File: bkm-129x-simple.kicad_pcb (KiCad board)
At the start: 2 copper layers, 105 x 89.3 mm, 52 parts, among them J1 YG1, J2 PBB1, J3 PRR1, J4 SYNC1, J5 Conn_02x32_Row_Letter_Last, Q1 DTC144EKA, U1 ADG1611, U2 THS7374, U3 arduino-nano-v3, U4 74LVC125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

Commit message: Added readme and some info on silkscreen
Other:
- board text added: "B-Y/B"
- board text added: "R-Y/R"
- board text added: "SYNC"
- board text added: "Y/G"
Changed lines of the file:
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@@
     (links 157)
     (no_connects 0)
-    (area 120.955999 61.773999 226.071501 151.205001)
+    (area 100.362599 61.652999 228.7352 151.453001)
     (thickness 1.6)
-    (drawings 10)
+    (drawings 14)
     (tracks 449)
     (zones 0)
@@
   (module bnc-tht:BNC-THT (layer F.Cu)
     (at 129.0066 73.4314)
-    (fp_text reference J1 (at 0 8.382) (layer F.SilkS)
+    (fp_text reference J1 (at 6.1214 -8.3439) (layer F.SilkS)
       (effects (font (size 1 1) (thickness 0.15)))
     )
@@
   (module bnc-tht:BNC-THT (layer F.Cu)
     (at 129.0066 95.4786)
-    (fp_text reference J2 (at 0 8.382) (layer F.SilkS)
+    (fp_text reference J2 (at 6.1214 -8.3566) (layer F.SilkS)
       (effects (font (size 1 1) (thickness 0.15)))
     )
@@
   (module bnc-tht:BNC-THT (layer F.Cu)
     (at 129.032 117.475)
-    (fp_text reference J3 (at 0 8.382) (layer F.SilkS)
+    (fp_text reference J3 (at 6.096 -8.382) (layer F.SilkS)
       (effects (font (size 1 1) (thickness 0.15)))
     )
@@
   (module bnc-tht:BNC-THT (layer F.Cu)
     (at 129.032 139.573)
-    (fp_text reference J4 (at 0 8.382) (layer F.SilkS)
+    (fp_text reference J4 (at 6.1595 -8.382) (layer F.SilkS)
       (effects (font (size 1 1) (thickness 0.15)))
     )
@@
     )
   )
+  (gr_text SYNC (at 133.096 148.463) (layer F.SilkS)
+    (effects (font (size 1.5 1.5) (thickness 0.3)))
+  )
+  (gr_text R-Y/R (at 132.1435 126.365) (layer F.SilkS)
+    (effects (font (size 1.5 1.5) (thickness 0.3)))
+  )
+  (gr_text B-Y/B (at 132.2705 104.4575) (layer F.SilkS)
+    (effects (font (size 1.5 1.5) (thickness 0.3)))
+  )
+  (gr_text Y/G (at 133.858 82.423) (layer F.SilkS)
+    (effects (font (size 1.5 1.5) (thickness 0.3)))
+  )
   (gr_text "(2020) Martin Hejnfelt (martin@hejnfelt.com)\nwww.immerhax.com" (at 171.9072 85.9536) (layer B.SilkS)

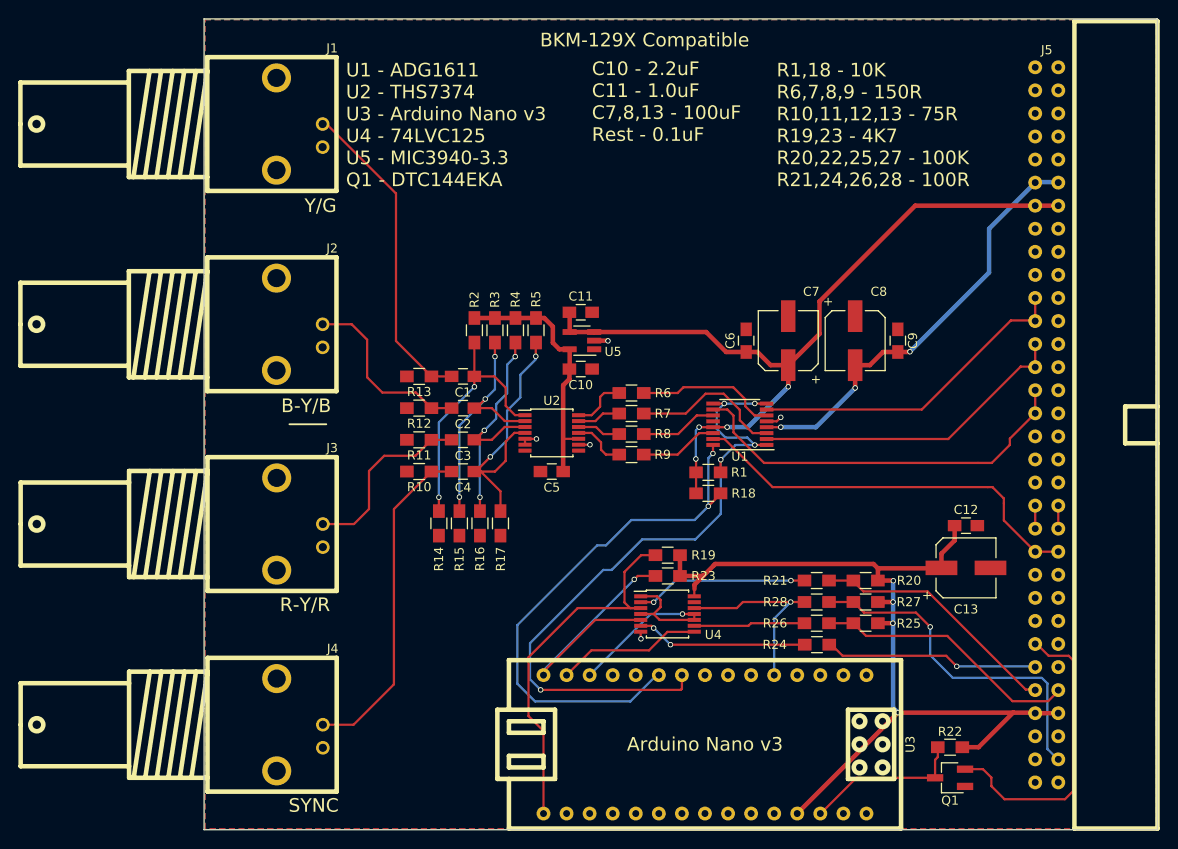
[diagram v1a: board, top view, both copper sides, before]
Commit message: Updated and fixed silkscreen BOM
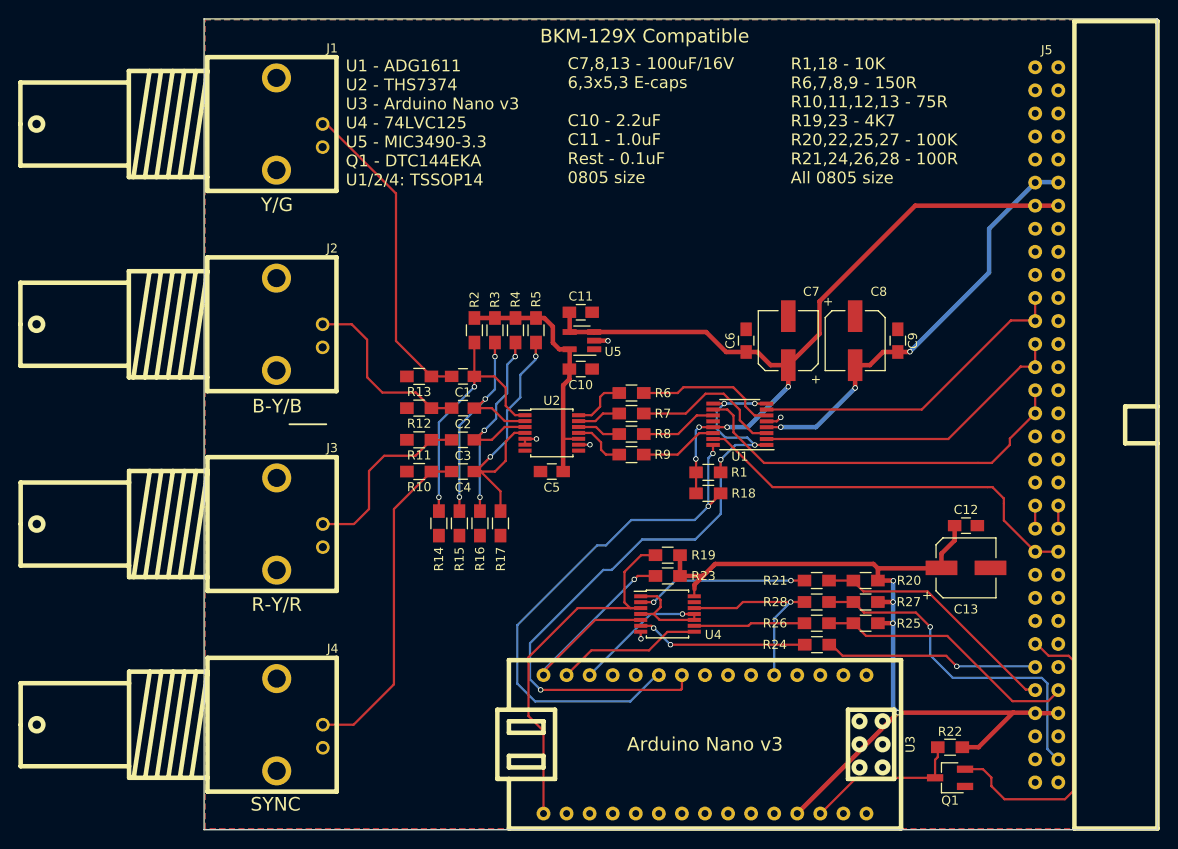
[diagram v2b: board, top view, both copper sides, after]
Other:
- board text added: "C7,8,13 - 100uF/16V 6,3x5,3 E-caps C10 - 2.2uF C11 - 1.0uF Rest - 0.1uF 0805 size"
- board text added: "R1,18 - 10K R6,7,8,9 - 150R R10,11,12,13 - 75R R19,23 - 4K7 R20,22,25,27 - 100K R21,24,26,28 - 100R All 0805 size"
- board text added: "U1 - ADG1611 U2 - THS7374 U3 - Arduino Nano v3 U4 - 74LVC125 U5 - MIC3490-3.3 Q1 - DTC144EKA U1/2/4: TSSOP14"
- board text removed: "C10 - 2.2uF C11 - 1.0uF C7,8,13 - 100uF Rest - 0.1uF"
- board text removed: "R1,18 - 10K R6,7,8,9 - 150R R10,11,12,13 - 75R R19,23 - 4K7 R20,22,25,27 - 100K R21,24,26,28 - 100R"
- board text removed: "U1 - ADG1611 U2 - THS7374 U3 - Arduino Nano v3 U4 - 74LVC125 U5 - MIC3940-3.3 Q1 - DTC144EKA"
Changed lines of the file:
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@@
     (links 157)
     (no_connects 0)
-    (area 100.362599 61.652999 228.7352 151.453001)
+    (area 120.955999 61.773999 226.071501 151.205001)
     (thickness 1.6)
     (drawings 14)
@@
     )
   )
-  (gr_text SYNC (at 133.096 148.463) (layer F.SilkS)
+  (gr_text SYNC (at 128.905 148.336) (layer F.SilkS)
     (effects (font (size 1.5 1.5) (thickness 0.3)))
   )
-  (gr_text R-Y/R (at 132.1435 126.365) (layer F.SilkS)
+  (gr_text R-Y/R (at 129.032 126.3396) (layer F.SilkS)
     (effects (font (size 1.5 1.5) (thickness 0.3)))
   )
-  (gr_text B-Y/B (at 132.2705 104.4575) (layer F.SilkS)
+  (gr_text B-Y/B (at 129.0828 104.4956) (layer F.SilkS)
     (effects (font (size 1.5 1.5) (thickness 0.3)))
   )
-  (gr_text Y/G (at 133.858 82.423) (layer F.SilkS)
+  (gr_text Y/G (at 129.0574 82.3214) (layer F.SilkS)
     (effects (font (size 1.5 1.5) (thickness 0.3)))
   )
@@
     (effects (font (size 1.5 1.5) (thickness 0.3)) (justify mirror))
   )
-  (gr_text "C10 - 2.2uF\nC11 - 1.0uF\nC7,8,13 - 100uF\nRest - 0.1uF" (at 163.7284 70.9676) (layer F.SilkS)
-    (effects (font (size 1.5 1.5) (thickness 0.3)) (justify left))
-  )
-  (gr_text "R1,18 - 10K\nR6,7,8,9 - 150R\nR10,11,12,13 - 75R\nR19,23 - 4K7\nR20,22,25,27 - 100K\nR21,24,26,28 - 100R" (at 184.0738 73.533) (layer F.SilkS)
-    (effects (font (size 1.5 1.5) (thickness 0.3)) (justify left))
-  )
-  (gr_text "U1 - ADG1611\nU2 - THS7374\nU3 - Arduino Nano v3\nU4 - 74LVC125\nU5 - MIC3940-3.3\nQ1 - DTC144EKA" (at 136.652 73.533) (layer F.SilkS)
-    (effects (font (size 1.5 1.5) (thickness 0.3)) (justify left))
-  )
-  (gr_text "BKM-129X Compatible" (at 169.545 64.1858) (layer F.SilkS)
+  (gr_text "C7,8,13 - 100uF/16V\n6,3x5,3 E-caps\n\nC10 - 2.2uF\nC11 - 1.0uF\nRest - 0.1uF\n0805 size\n" (at 161.0614 73.0504) (layer F.SilkS)
+    (effects (font (size 1.3 1.3) (thickness 0.25)) (justify left))
+  )
+  (gr_text "R1,18 - 10K\nR6,7,8,9 - 150R\nR10,11,12,13 - 75R\nR19,23 - 4K7\nR20,22,25,27 - 100K\nR21,24,26,28 - 100R\nAll 0805 size" (at 185.6232 73.0758) (layer F.SilkS)
+    (effects (font (size 1.3 1.3) (thickness 0.25)) (justify left))
+  )
+  (gr_text "U1 - ADG1611\nU2 - THS7374\nU3 - Arduino Nano v3\nU4 - 74LVC125\nU5 - MIC3490-3.3\nQ1 - DTC144EKA\nU1/2/4: TSSOP14" (at 136.6266 73.3044) (layer F.SilkS)
+    (effects (font (size 1.3 1.3) (thickness 0.25)) (justify left))
+  )
+  (gr_text "BKM-129X Compatible" (at 169.545 63.754) (layer F.SilkS)
     (effects (font (size 1.5 1.5) (thickness 0.3)))
   )

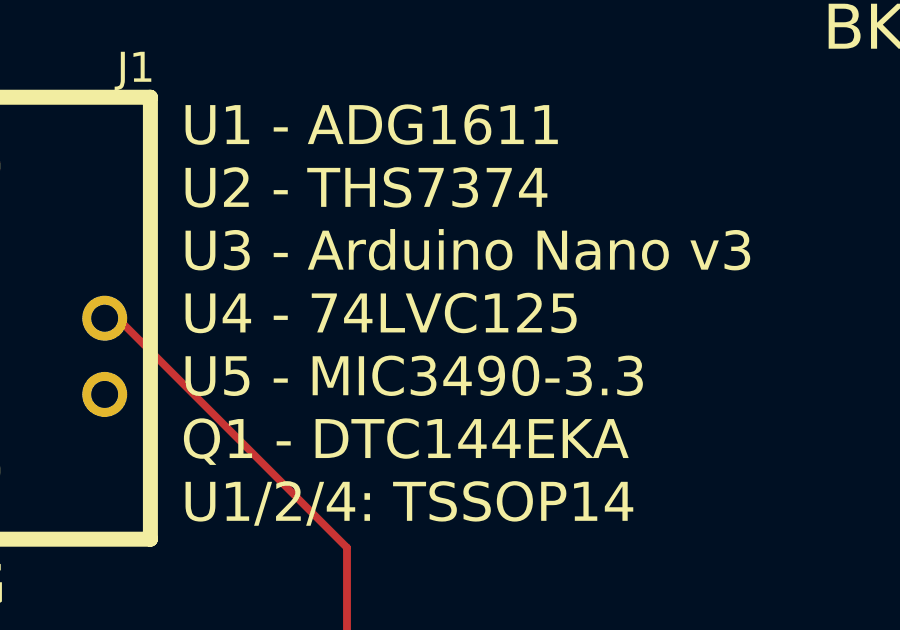
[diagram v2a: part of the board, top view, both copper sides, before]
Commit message: Fixed more BOM mistakes
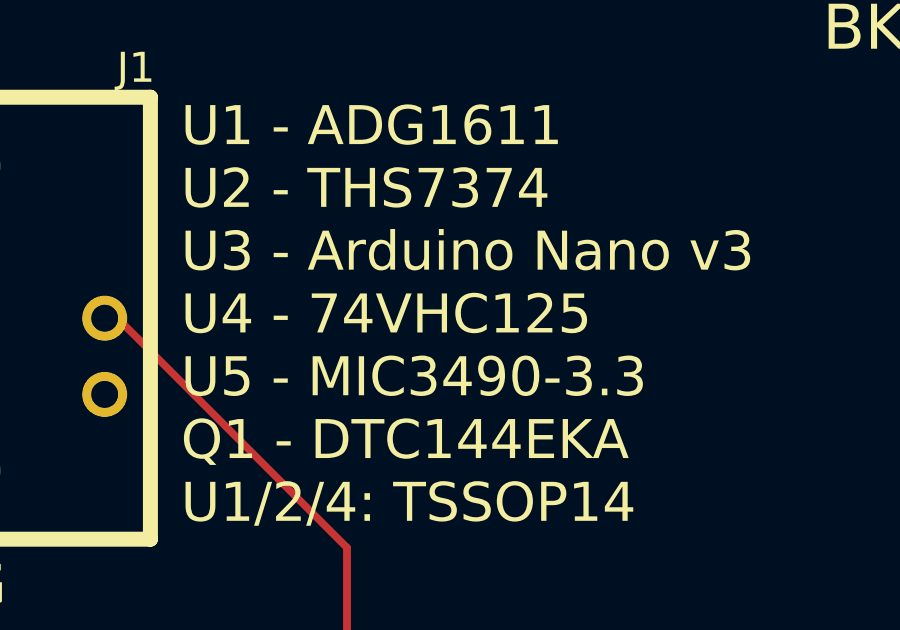
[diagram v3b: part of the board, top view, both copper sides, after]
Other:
- board text added: "U1 - ADG1611 U2 - THS7374 U3 - Arduino Nano v3 U4 - 74VHC125 U5 - MIC3490-3.3 Q1 - DTC144EKA U1/2/4: TSSOP14"
- board text removed: "U1 - ADG1611 U2 - THS7374 U3 - Arduino Nano v3 U4 - 74LVC125 U5 - MIC3490-3.3 Q1 - DTC144EKA U1/2/4: TSSOP14"
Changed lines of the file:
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@@
     (links 157)
     (no_connects 0)
-    (area 120.955999 61.773999 226.071501 151.205001)
+    (area 100.362599 61.652999 228.7352 151.453001)
     (thickness 1.6)
     (drawings 14)
@@
     (effects (font (size 1.3 1.3) (thickness 0.25)) (justify left))
   )
-  (gr_text "U1 - ADG1611\nU2 - THS7374\nU3 - Arduino Nano v3\nU4 - 74LVC125\nU5 - MIC3490-3.3\nQ1 - DTC144EKA\nU1/2/4: TSSOP14" (at 136.6266 73.3044) (layer F.SilkS)
+  (gr_text "U1 - ADG1611\nU2 - THS7374\nU3 - Arduino Nano v3\nU4 - 74VHC125\nU5 - MIC3490-3.3\nQ1 - DTC144EKA\nU1/2/4: TSSOP14" (at 136.6266 73.3044) (layer F.SilkS)
     (effects (font (size 1.3 1.3) (thickness 0.25)) (justify left))
   )

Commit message: Fixed MIC3940 -> MIC3490
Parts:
- U5: value MIC3940 -> MIC3490-3.3
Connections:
- J5 pad 10b: Net-(J5-Pad10b) -> (no net)
- J5 pad 17a: Net-(J5-Pad17a) -> (no net)
- J5 pad 18a: Net-(J5-Pad18a) -> (no net)
- J5 pad 18b: Net-(J5-Pad18b) -> (no net)
- J5 pad 19a: Net-(J5-Pad19a) -> (no net)
- J5 pad 19b: Net-(J5-Pad19b) -> (no net)
- J5 pad 23b: Net-(J5-Pad23b) -> (no net)
- J5 pad 24b: Net-(J5-Pad24b) -> (no net)
- J5 pad 25a: Net-(J5-Pad25a) -> (no net)
- J5 pad 25b: Net-(J5-Pad25b) -> (no net)
- J5 pad 26a: Net-(J5-Pad26a) -> (no net)
- J5 pad 27a: Net-(J5-Pad27a) -> (no net)
- J5 pad 2a: Net-(J5-Pad2a) -> (no net)
- J5 pad 2b: Net-(J5-Pad2b) -> (no net)
- J5 pad 31b: Net-(J5-Pad31b) -> (no net)
- J5 pad 4a: Net-(J5-Pad4a) -> (no net)
- J5 pad 4b: Net-(J5-Pad4b) -> (no net)
- J5 pad 5a: Net-(J5-Pad5a) -> (no net)
- J5 pad 5b: Net-(J5-Pad5b) -> (no net)
- J5 pad 8b: Net-(J5-Pad8b) -> (no net)
- J5 pad 9b: Net-(J5-Pad9b) -> (no net)
- U2 pad 7: Net-(U2-Pad7) -> (no net)
- U2 pad 8: Net-(U2-Pad8) -> (no net)
- U3 pad 1: Net-(U3-Pad1) -> (no net)
- U3 pad 11: Net-(U3-Pad11) -> (no net)
- U3 pad 12: Net-(U3-Pad12) -> (no net)
- U3 pad 17: Net-(U3-Pad17) -> (no net)
- U3 pad 18: Net-(U3-Pad18) -> (no net)
- U3 pad 19: Net-(U3-Pad19) -> (no net)
- U3 pad 2: Net-(U3-Pad2) -> (no net)
- U3 pad 20: Net-(U3-Pad20) -> (no net)
- U3 pad 21: Net-(U3-Pad21) -> (no net)
- U3 pad 22: Net-(U3-Pad22) -> (no net)
- U3 pad 23: Net-(U3-Pad23) -> (no net)
- U3 pad 24: Net-(U3-Pad24) -> (no net)
- U3 pad 25: Net-(U3-Pad25) -> (no net)
- U3 pad 26: Net-(U3-Pad26) -> (no net)
- U3 pad 3: Net-(U3-Pad3) -> (no net)
- U3 pad 30: Net-(U3-Pad30) -> (no net)
- U3 pad 6: Net-(U3-Pad6) -> (no net)
- U3 pad 7: Net-(U3-Pad7) -> (no net)
- U3 pad 8: Net-(U3-Pad8) -> (no net)
- U5 pad 1: Net-(U5-Pad1) -> (no net)

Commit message: Added revision, compatibility and credits
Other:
- board text added: "R1,18 - 10K R6,7,8, - 150R R9 - 0R (or jumper) R10,11,12,13 - 75R R19,23 - 4K7 R20,22,25,27 - 100K R21,24,26,28 - 100R All 0805 size"
- board text added: "Rev. A"
- board text removed: "R1,18 - 10K R6,7,8,9 - 150R R10,11,12,13 - 75R R19,23 - 4K7 R20,22,25,27 - 100K R21,24,26,28 - 100R All 0805 size"
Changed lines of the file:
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@@
     (links 157)
     (no_connects 0)
-    (area 120.955999 61.773999 226.071501 151.205001)
+    (area 100.362599 61.652999 228.7352 151.453001)
     (thickness 1.6)
-    (drawings 14)
+    (drawings 15)
     (tracks 449)
     (zones 0)
@@
     )
   )
+  (gr_text "Rev. A" (at 144.4625 148.971) (layer F.SilkS)
+    (effects (font (size 1.5 1.5) (thickness 0.3)))
+  )
   (gr_text SYNC (at 128.905 148.336) (layer F.SilkS)
     (effects (font (size 1.5 1.5) (thickness 0.3)))
@@
     (effects (font (size 1.3 1.3) (thickness 0.25)) (justify left))
   )
-  (gr_text "R1,18 - 10K\nR6,7,8,9 - 150R\nR10,11,12,13 - 75R\nR19,23 - 4K7\nR20,22,25,27 - 100K\nR21,24,26,28 - 100R\nAll 0805 size" (at 185.6232 73.0758) (layer F.SilkS)
+  (gr_text "R1,18 - 10K\nR6,7,8, - 150R\nR9 - 0R (or jumper)\nR10,11,12,13 - 75R\nR19,23 - 4K7\nR20,22,25,27 - 100K\nR21,24,26,28 - 100R\nAll 0805 size" (at 185.6105 74.1045) (layer F.SilkS)
     (effects (font (size 1.3 1.3) (thickness 0.25)) (justify left))
   )

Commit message: Fixed R9 to 0 Ohm on PCB also
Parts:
- R9: value 150R -> 0R
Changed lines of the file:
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@@
     (links 157)
     (no_connects 0)
-    (area 100.362599 61.652999 228.7352 151.453001)
+    (area 120.955999 61.773999 226.071501 151.205001)
     (thickness 1.6)
     (drawings 15)
@@
       (effects (font (size 1 1) (thickness 0.15)))
     )
-    (fp_text value 150R (at 0 1.75 180) (layer F.Fab)
-      (effects (font (size 1 1) (thickness 0.15)))
-    )
+    (fp_text value 0R (at 0 1.75 180) (layer F.Fab)
+      (effects (font (size 1 1) (thickness 0.15)))
+    )

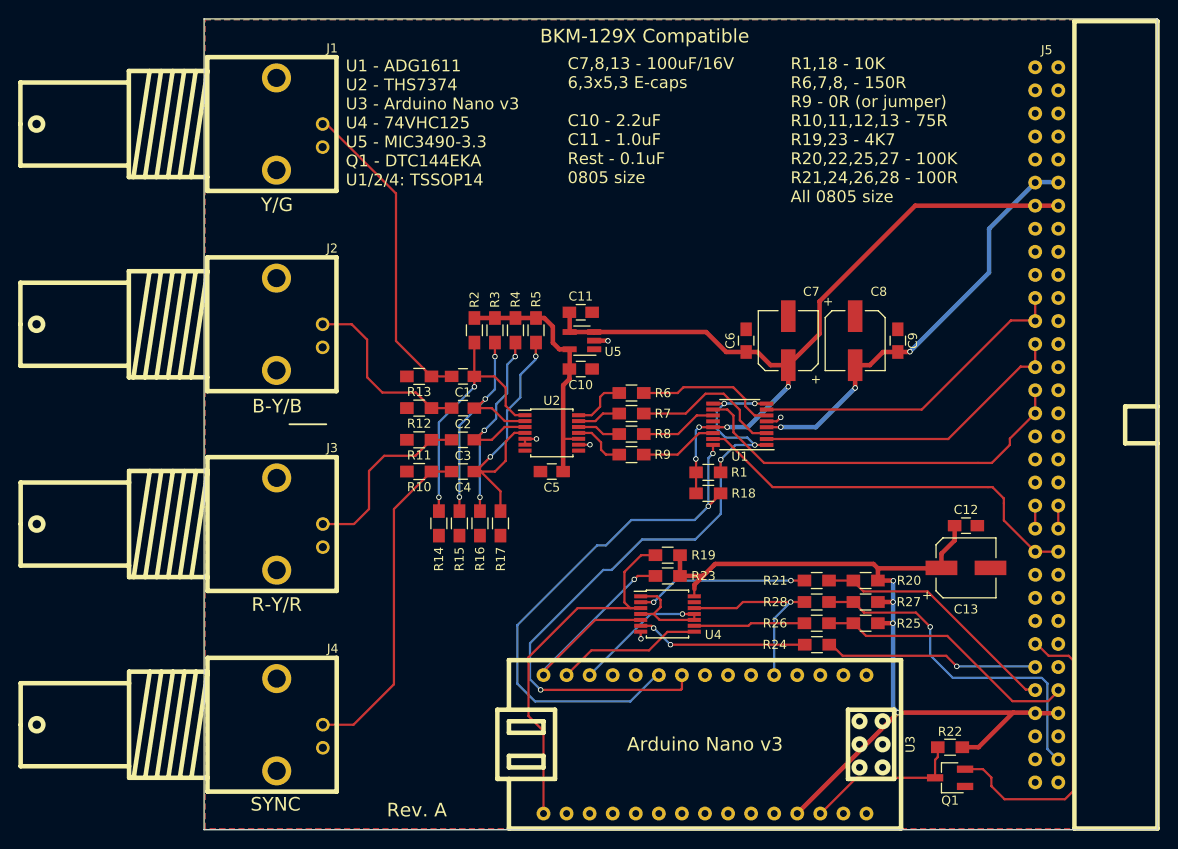
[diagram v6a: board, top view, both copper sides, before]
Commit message: Added overbrightness fix
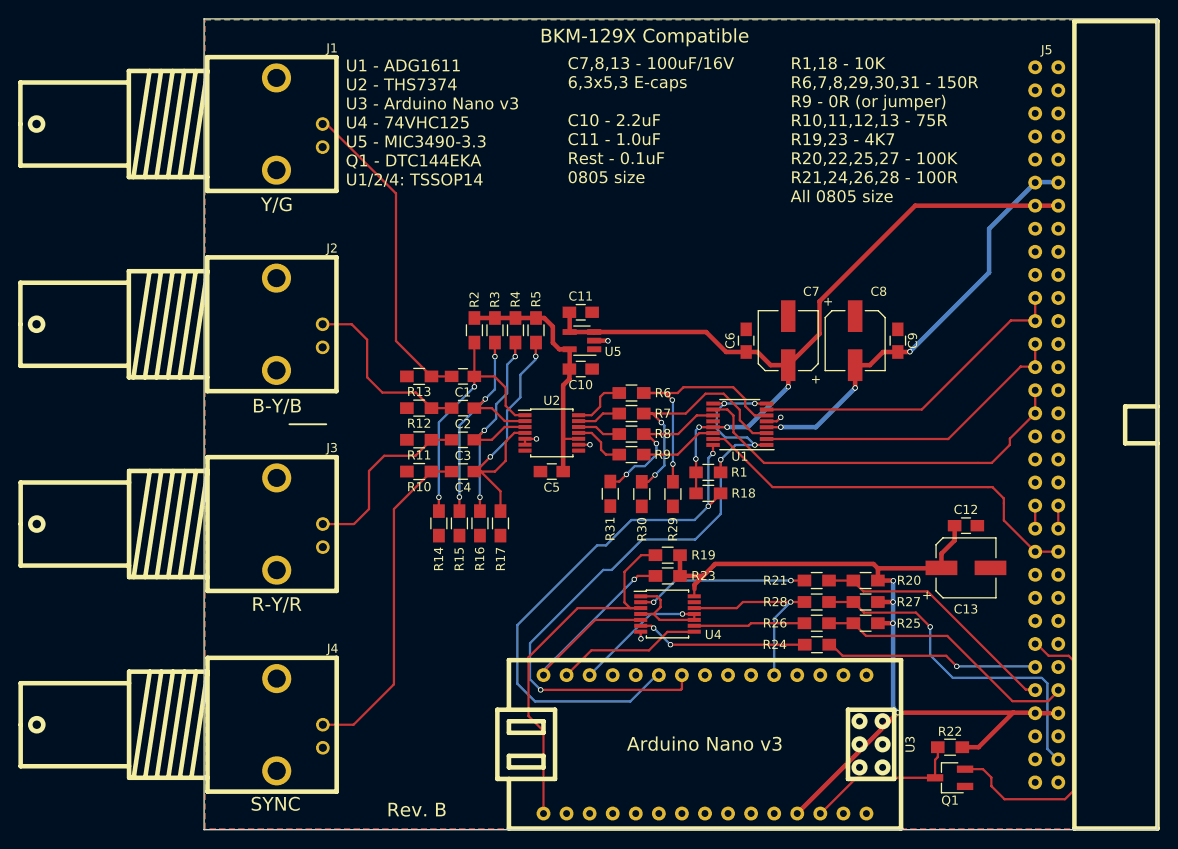
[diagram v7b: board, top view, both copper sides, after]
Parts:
- added R29: 150R, Resistors_SMD:R_0805_HandSoldering, F.Cu at (172.7, 114.2)
- added R30: 150R, Resistors_SMD:R_0805_HandSoldering, F.Cu at (169.2, 114.2)
- added R31: 150R, Resistors_SMD:R_0805_HandSoldering, F.Cu at (165.8, 114.1)
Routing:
- net Net-(R29-Pad1): track 15.5 -> 28.0 mm, vias 0 -> 2
- net Net-(R30-Pad1): track 16.9 -> 27.4 mm, vias 0 -> 2
- net Net-(R31-Pad1): track 8.48 -> 17.8 mm, vias 0 -> 2
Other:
- board text added: "R1,18 - 10K R6,7,8,29,30,31 - 150R R9 - 0R (or jumper) R10,11,12,13 - 75R R19,23 - 4K7 R20,22,25,27 - 100K R21,24,26,28 - 100R All 0805 size"
- board text added: "Rev. B"
- board text removed: "R1,18 - 10K R6,7,8, - 150R R9 - 0R (or jumper) R10,11,12,13 - 75R R19,23 - 4K7 R20,22,25,27 - 100K R21,24,26,28 - 100R All 0805 size"
- board text removed: "Rev. A"
